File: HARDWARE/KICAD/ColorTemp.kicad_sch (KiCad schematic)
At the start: 2 parts, among them U1 CH32V003F4U6

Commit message: Advancing on parts creation.
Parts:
- added R1, R2, R3: 1K 1%, ColorTemp:R_0603_1608Metric, symbol ColorTemp:R0603 1K 1% 75V 100mW
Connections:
- net +5V: now also R1.1, R2.1, R3.1

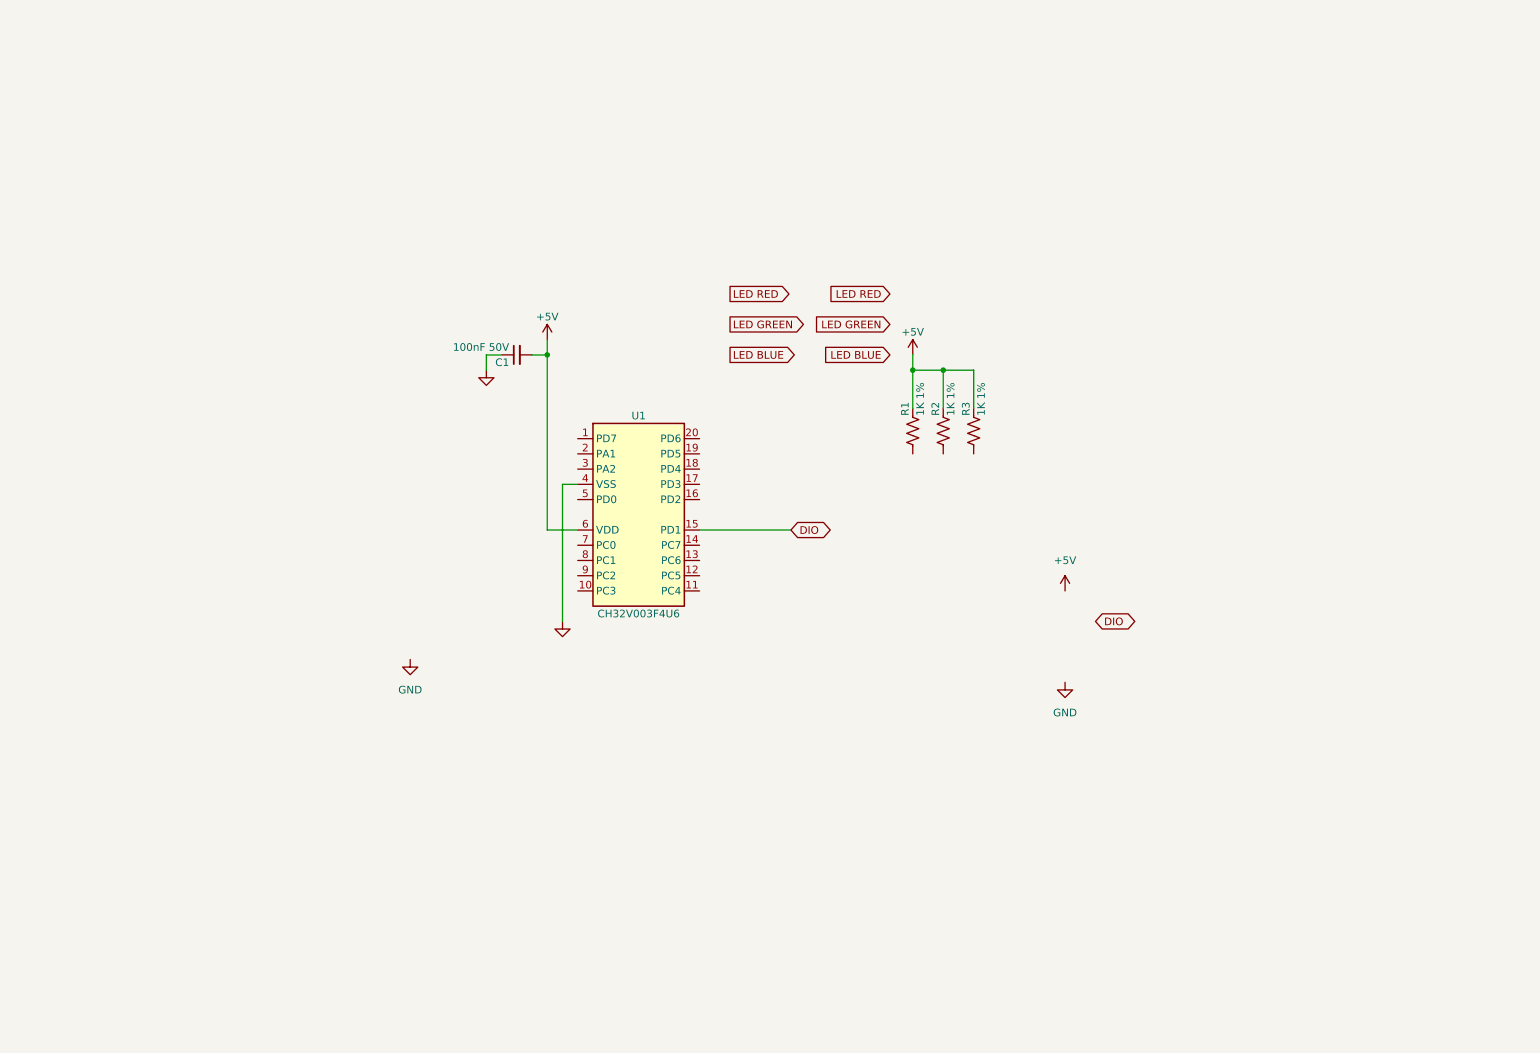
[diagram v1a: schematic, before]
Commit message: Added most of the components. Recently project started crashing on PCB, when I press X to route. I'll try to restore a backup.
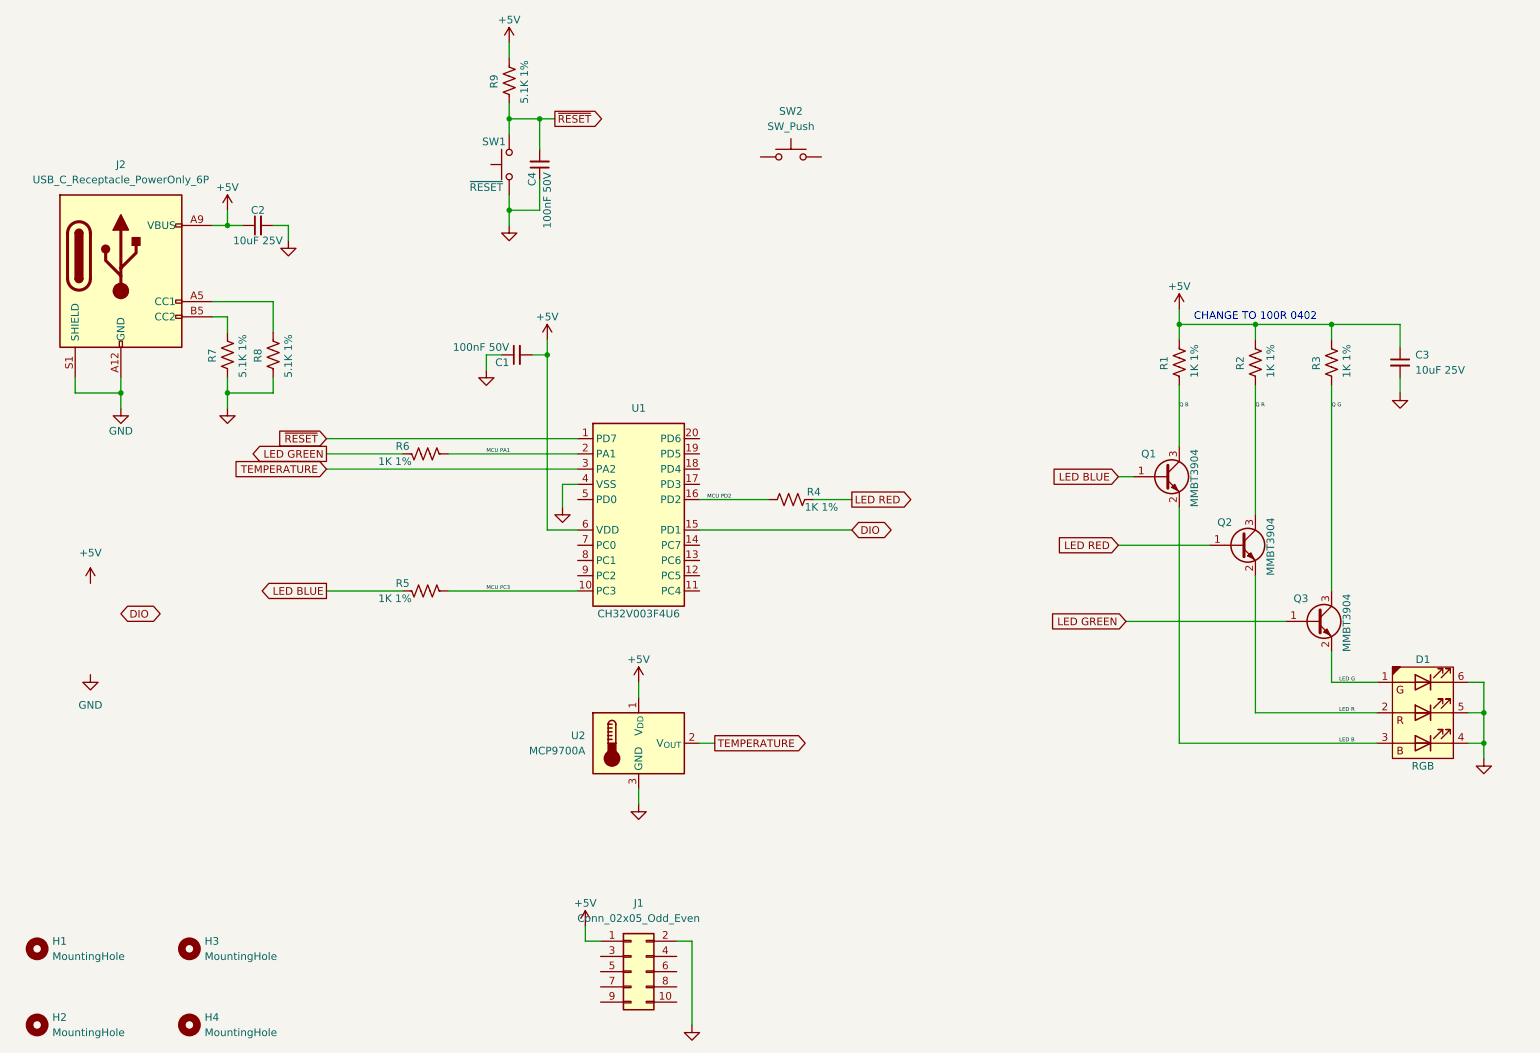
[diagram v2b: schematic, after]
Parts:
- added C2, C3: 10uF 25V, ColorTemp:C_0805_2012Metric, symbol ColorTemp:C0805 10uF 25V X5R
- added C4: 100nF 50V, ColorTemp:C_0402_1005Metric, symbol ColorTemp:C0402 100nF 50V X7R
- added D1: RGB, ColorTemp:LED_RGB_5050-6, symbol ColorTemp:LED RGB 5050
- added H1, H2, H3, H4: MountingHole, ColorTemp:MountingHole_3.2mm_M3, symbol ColorTemp:MountingHole
- added J1: Conn_02x05_Odd_Even, ColorTemp:PinHeader_2x05_P2.54mm_Vertical, symbol ColorTemp:Conn_02x05_Odd_Even
- added J2: USB_C_Receptacle_PowerOnly_6P, ColorTemp:USB_C_Receptacle_GCT_USB4125-xx-x-0190_6P_TopMnt_Horizontal, symbol ColorTemp:USB_C_Receptacle_PowerOnly_6P
- added Q1, Q2, Q3: MMBT3904, ColorTemp:SOT-23, symbol ColorTemp:MMBT3904
- added R4, R5, R6: 1K 1%, ColorTemp:R_0402_1005Metric, symbol ColorTemp:R0402 1K 1% 50V 62.5mW
- added R7, R8, R9: 5.1K 1%, ColorTemp:R_0402_1005Metric, symbol ColorTemp:R0402 5.1K 1% 50V 62.5mW
- added SW1: ~{RESET}, symbol ColorTemp:SW_Push
- added SW2: SW_Push, symbol ColorTemp:SW_Push
- added U2: MCP9700A, ColorTemp:SOT-23, symbol ColorTemp:MCP9700AT-E/TT
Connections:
- net +5V: now also C2.1, C3.1, J1.1 (Pin_1), J2.A9 (VBUS), J2.B9 (VBUS), R9.1, U2.1 (V_{DD})
- net GND: now also C2.2, C3.2, C4.1, D1.4 (K), D1.5 (K), D1.6 (K), J1.2 (Pin_2), J2.A12 (GND), J2.B12 (GND), J2.S1 (SHIELD), R7.2, R8.2, SW1.1, U2.3 (GND)
- net LED BLUE: now also Q1.1 (B), R5.2
- net LED GREEN: now also Q3.1 (B), R6.2
- net LED RED: now also Q2.1 (B), R4.2
- net Q R: now reaches R2.2
- net Q R: now also Q2.3 (C)
- net ~{RESET}: now reaches U1.1 (PD7)
- net ~{RESET}: now also C4.2, R9.2, SW1.2
- net MCU PC3: now reaches U1.10 (PC3)
- net MCU PC3: now also R5.1
- net MCU PD2: now reaches U1.16 (PD2)
- net MCU PD2: now also R4.1
- net MCU PA1: now reaches U1.2 (PA1)
- net MCU PA1: now also R6.1
- net TEMPERATURE: now reaches U1.3 (PA2)
- net TEMPERATURE: now also U2.2 (V_{OUT})
- net Q B: now reaches R1.2
- net Q B: now also Q1.3 (C)
- net Q G: now reaches R3.2
- net Q G: now also Q3.3 (C)
- new net: J2.A5 (CC1), R8.1
- new net: J2.B5 (CC2), R7.1
- new net LED B: D1.3 (A), Q1.2 (E)
- new net LED G: D1.1 (A), Q3.2 (E)
- new net LED R: D1.2 (A), Q2.2 (E)
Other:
- note added: "CHANGE TO 100R 0402"
- moved on the sheet: R1, R2, R3

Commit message: Restored working project.
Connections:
- net +5V: now also J1.2 (Pin_2); no longer J1.1 (Pin_1)
- net GND: now also J1.1 (Pin_1); no longer J1.2 (Pin_2)
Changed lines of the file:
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@@
-	(wire
-		(pts
-			(xy 135.89 186.69) (xy 135.89 172.72)
-		)
-		(stroke
-			(width 0)
-			(type default)
-		)
-	)
 	(wire
 		(pts
@@
 	(wire
 		(pts
+			(xy 140.97 172.72) (xy 140.97 168.91)
+		)
+		(stroke
+			(width 0)
+			(type default)
+		)
+	)
+	(wire
+		(pts
 			(xy 110.49 45.72) (xy 110.49 50.8)
 		)
@@
 	(wire
 		(pts
-			(xy 135.89 172.72) (xy 133.35 172.72)
-		)
-		(stroke
-			(width 0)
-			(type default)
-		)
-	)
-	(wire
-		(pts
 			(xy 116.84 104.14) (xy 111.76 104.14)
 		)
@@
 	(wire
 		(pts
-			(xy 118.11 170.18) (xy 118.11 172.72)
-		)
-		(stroke
-			(width 0)
-			(type default)
-		)
-	)
-	(wire
-		(pts
 			(xy 109.22 74.93) (xy 111.76 74.93)
 		)
@@
 	(wire
 		(pts
+			(xy 116.84 172.72) (xy 120.65 172.72)
+		)
+		(stroke
+			(width 0)
+			(type default)
+		)
+	)
+	(wire
+		(pts
 			(xy 55.88 53.34) (xy 58.42 53.34)
 		)
@@
 	(wire
 		(pts
+			(xy 133.35 172.72) (xy 140.97 172.72)
+		)
+		(stroke
+			(width 0)
+			(type default)
+		)
+	)
+	(wire
+		(pts
 			(xy 242.57 80.01) (xy 242.57 114.3)
 		)
@@
 	(wire
 		(pts
-			(xy 118.11 172.72) (xy 120.65 172.72)
-		)
-		(stroke
-			(width 0)
-			(type default)
-		)
-	)
-	(wire
-		(pts
 			(xy 74.93 88.9) (xy 116.84 88.9)
 		)
@@
 		(pts
 			(xy 66.04 66.04) (xy 66.04 71.12)
+		)
+		(stroke
+			(width 0)
+			(type default)
+		)
+	)
+	(wire
+		(pts
+			(xy 116.84 186.69) (xy 116.84 172.72)
 		)
 		(stroke
@@
 	(symbol
 		(lib_id "ColorTemp:+5V")
-		(at 118.11 170.18 0)
+		(at 140.97 168.91 0)
 		(unit 1)
 		(exclude_from_sim no)
@@
 		(dnp no)
 		(property "Reference" "#PWR017"
-			(at 118.11 173.99 0)
+			(at 140.97 172.72 0)
 			(effects
 				(font
@@
 		)
 		(property "Value" "+5V"
-			(at 118.11 166.37 0)
+			(at 140.97 165.1 0)
 			(effects
 				(font
@@
 		)
 		(property "Footprint" ""
-			(at 118.11 170.18 0)
+			(at 140.97 168.91 0)
 			(effects
 				(font
@@
 		)
 		(property "Datasheet" ""
-			(at 118.11 170.18 0)
+			(at 140.97 168.91 0)
 			(effects
 				(font
@@
 		)
 		(property "Description" "Power symbol creates a global label with name \"+5V\""
-			(at 118.11 170.18 0)
+			(at 140.97 168.91 0)
 			(effects
 				(font
@@
 	(symbol
 		(lib_id "ColorTemp:GND")
-		(at 135.89 186.69 0)
+		(at 116.84 186.69 0)
 		(unit 1)
 		(exclude_from_sim no)
@@
 		(fields_autoplaced yes)
 		(property "Reference" "#PWR018"
-			(at 135.89 193.04 0)
+			(at 116.84 193.04 0)
 			(effects
 				(font
@@
 		)
 		(property "Value" "GND"
-			(at 135.89 191.77 0)
+			(at 116.84 191.77 0)
 			(effects
 				(font
@@
 		)
 		(property "Footprint" ""
-			(at 135.89 186.69 0)
+			(at 116.84 186.69 0)
 			(effects
 				(font
@@
 		)
 		(property "Datasheet" ""
-			(at 135.89 186.69 0)
+			(at 116.84 186.69 0)
 			(effects
 				(font
@@
 		)
 		(property "Description" "Power symbol creates a global label with name \"GND\" , ground"
-			(at 135.89 186.69 0)
-			(effects
-				(font
+			(at 116.84 186.69 0)
+			(effects
+				(font

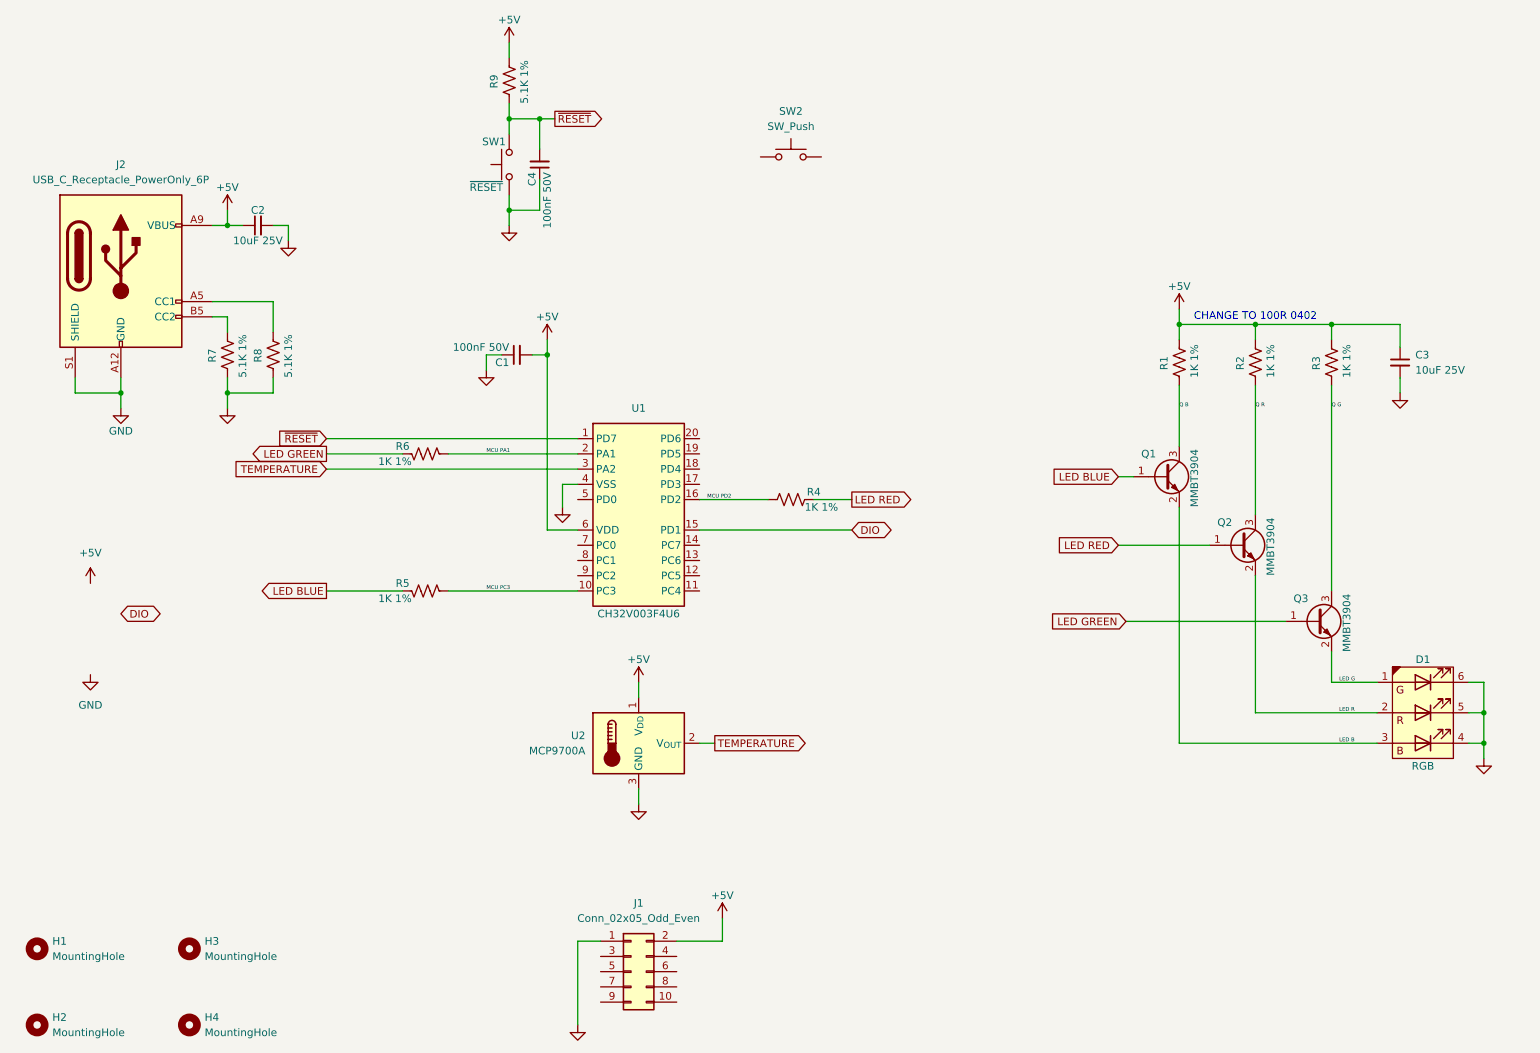
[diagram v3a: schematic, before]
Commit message: Project restored and back to normal. Added signals to external connector.
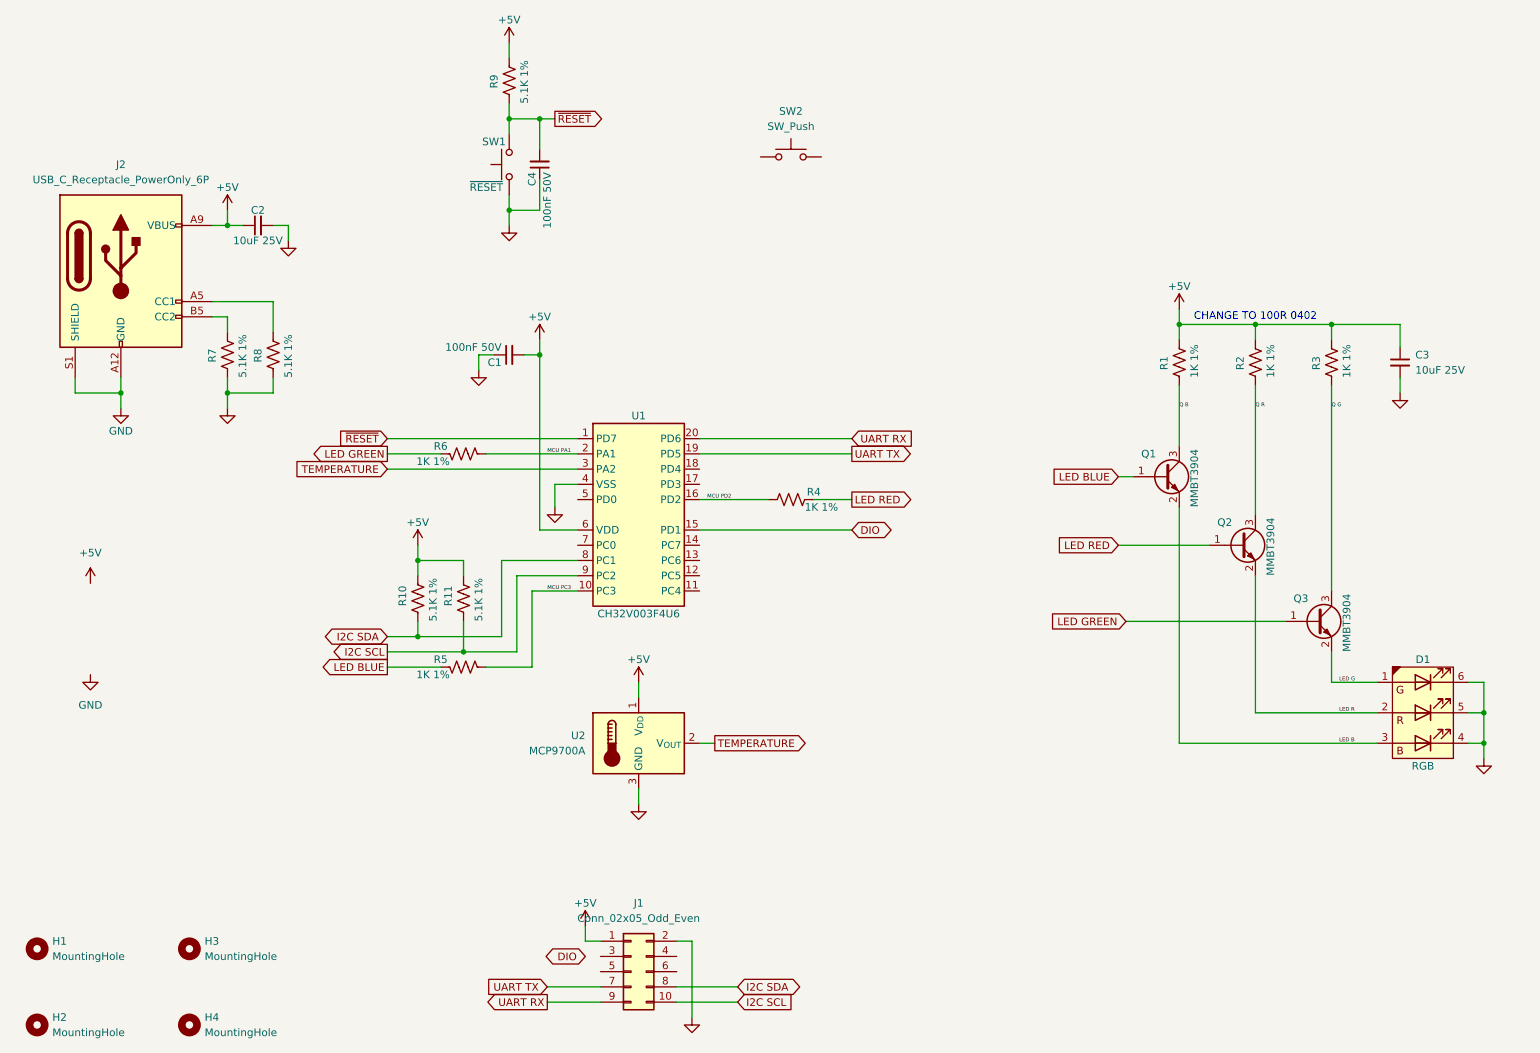
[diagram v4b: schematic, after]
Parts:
- added R10, R11: 5.1K 1%, ColorTemp:R_0402_1005Metric, symbol ColorTemp:R0402 5.1K 1% 50V 62.5mW
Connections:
- net +5V: now also J1.1 (Pin_1), R10.1, R11.1; no longer J1.2 (Pin_2)
- net GND: now also J1.2 (Pin_2); no longer J1.1 (Pin_1)
- net I2C SCL: now reaches J1.10 (Pin_10)
- net I2C SCL: now also U1.9 (PC2), R11.2
- net UART TX: now reaches J1.7 (Pin_7)
- net UART TX: now also U1.19 (PD5)
- net I2C SDA: now reaches J1.8 (Pin_8)
- net I2C SDA: now also U1.8 (PC1), R10.2
- net UART RX: now reaches J1.9 (Pin_9)
- net UART RX: now also U1.20 (PD6)
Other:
- moved on the sheet: C1, R5, R6
